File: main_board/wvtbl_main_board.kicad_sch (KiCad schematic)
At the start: 12 parts, among them J101 V/Oct, J102 X, J103 Y, J104 Out, J105 Conn_02x08_Odd_Even

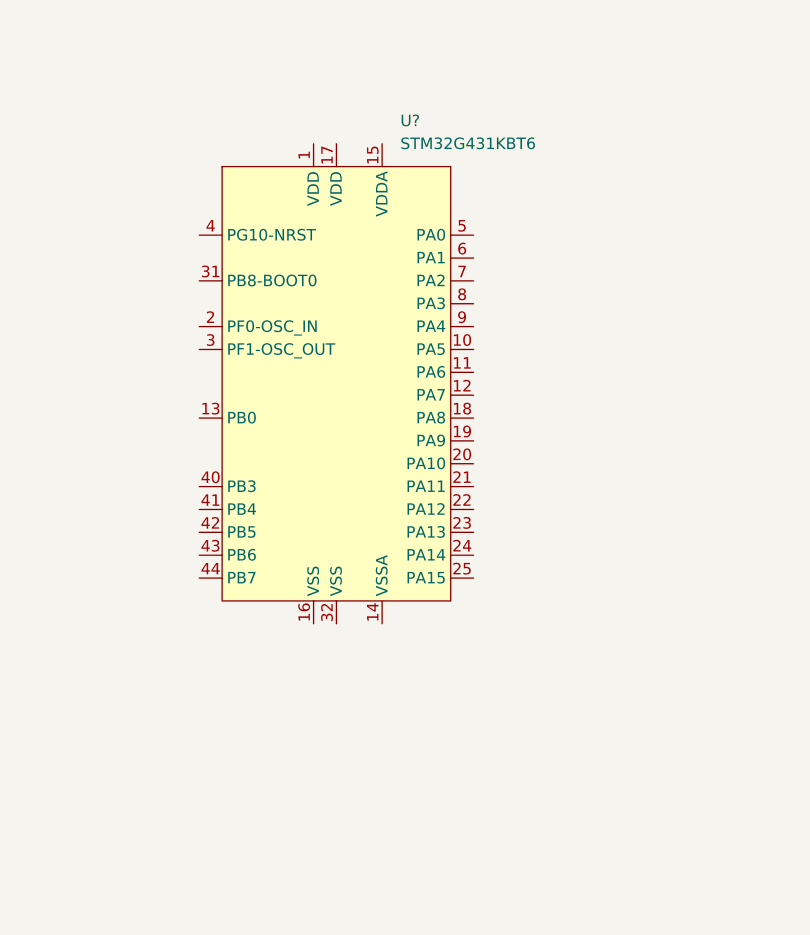
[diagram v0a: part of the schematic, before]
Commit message: 6HP Compute module
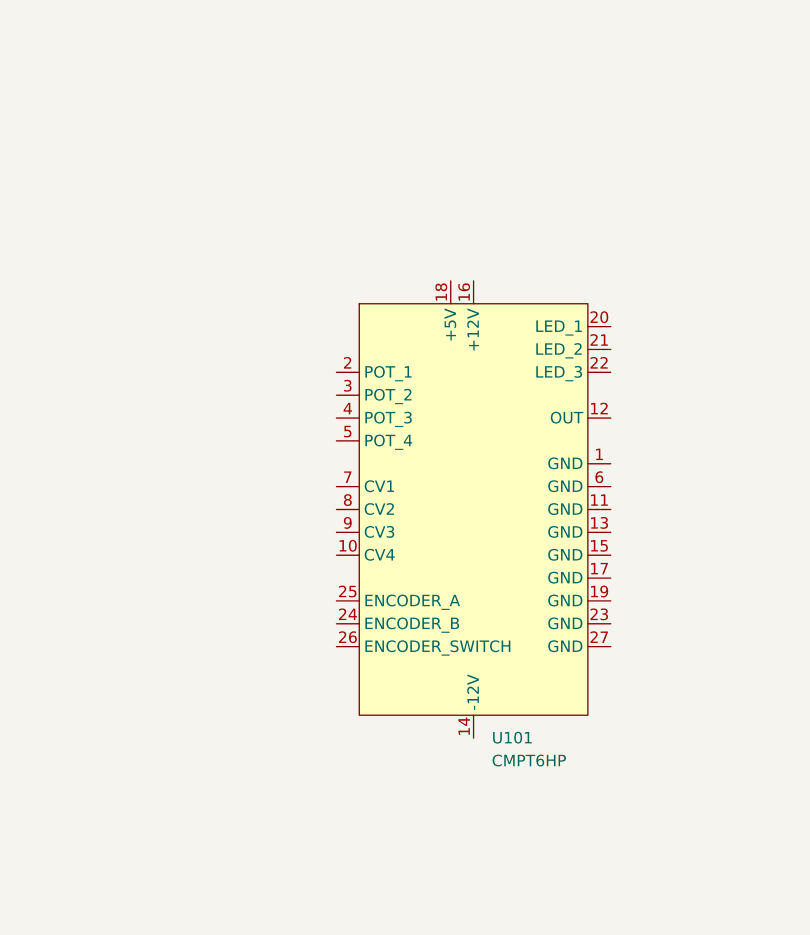
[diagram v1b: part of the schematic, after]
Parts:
- removed U?: STM32G431KBT6, Package_QFP:LQFP-32_7x7mm_P0.8mm, symbol WITNS_ST:STM32G431KBT6
- added U101: CMPT6HP, WITNS:CMPT6HP, symbol WITNS_EURORACK:CMPT6HP
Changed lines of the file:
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@@
     (pin "TN")
   )
-  (symbol (lib_id "Device:R_Potentiometer_Small") (at 106.68 115.57 0) (unit 1)
-    (in_bom yes) (on_board yes) (fields_autoplaced)
-    (property "Reference" "RV102" (id 0) (at 104.14 114.2999 0)
-      (effects (font (size 1.27 1.27)) (justify right))
-    )
-    (property "Value" "100k" (id 1) (at 104.14 116.8399 0)
-      (effects (font (size 1.27 1.27)) (justify right))
-    )
-    (property "Footprint" "WITNS:Potentiometer_Alpha_RD901F-40-00D_Single_Vertical" (id 2) (at 106.68 115.57 0)
-      (effects (font (size 1.27 1.27)) hide)
-    )
-    (property "Datasheet" "~" (id 3) (at 106.68 115.57 0)
-      (effects (font (size 1.27 1.27)) hide)
-    )
-    (pin "1")
-    (pin "2")
-    (pin "3")
-  )
-  (symbol (lib_id "Connector_Generic:Conn_02x08_Odd_Even") (at 50.8 151.13 0) (unit 1)
-    (in_bom yes) (on_board yes) (fields_autoplaced)
-    (property "Reference" "J105" (id 0) (at 52.07 137.16 0))
-    (property "Value" "Conn_02x08_Odd_Even" (id 1) (at 52.07 139.7 0))
-    (property "Footprint" "Connector_PinHeader_2.54mm:PinHeader_2x08_P2.54mm_Vertical_SMD" (id 2) (at 50.8 151.13 0)
-      (effects (font (size 1.27 1.27)) hide)
-    )
-    (property "Datasheet" "~" (id 3) (at 50.8 151.13 0)
-      (effects (font (size 1.27 1.27)) hide)
-    )
-    (pin "1")
-    (pin "10")
-    (pin "11")
-    (pin "12")
-    (pin "13")
-    (pin "14")
-    (pin "15")
-    (pin "16")
-    (pin "2")
-    (pin "3")
-    (pin "4")
-    (pin "5")
-    (pin "6")
-    (pin "7")
-    (pin "8")
-    (pin "9")
-  )
-  (symbol (lib_id "Connector:AudioJack2_SwitchT") (at 120.65 138.43 0) (unit 1)
-    (in_bom yes) (on_board yes) (fields_autoplaced)
-    (property "Reference" "J102" (id 0) (at 120.015 129.54 0))
-    (property "Value" "X" (id 1) (at 120.015 132.08 0))
-    (property "Footprint" "WITNS:Jack_3.5mm_QingPu_WQP-PJ398SM_Vertical_CircularHoles" (id 2) (at 120.65 138.43 0)
-      (effects (font (size 1.27 1.27)) hide)
-    )
-    (property "Datasheet" "~" (id 3) (at 120.65 138.43 0)
-      (effects (font (size 1.27 1.27)) hide)
-    )
-    (pin "S")
-    (pin "T")
-    (pin "TN")
-  )
-  (symbol (lib_id "WITNS_ST:STM32G431KBT6") (at 182.88 57.15 0) (unit 1)
-    (in_bom yes) (on_board yes) (fields_autoplaced)
-    (property "Reference" "U?" (id 0) (at 189.9794 27.94 0)
+  (symbol (lib_id "WITNS_EURORACK:CMPT6HP") (at 198.12 52.07 0) (unit 1)
+    (in_bom yes) (on_board yes) (fields_autoplaced)
+    (property "Reference" "U101" (id 0) (at 200.1394 96.52 0)
       (effects (font (size 1.27 1.27)) (justify left))
     )
-    (property "Value" "STM32G431KBT6" (id 1) (at 189.9794 30.48 0)
+    (property "Value" "CMPT6HP" (id 1) (at 200.1394 99.06 0)
       (effects (font (size 1.27 1.27)) (justify left))
     )
-    (property "Footprint" "Package_QFP:LQFP-32_7x7mm_P0.8mm" (id 2) (at 182.88 96.52 0)
-      (effects (font (size 1.27 1.27)) hide)
-    )
-    (property "Datasheet" "" (id 3) (at 182.88 99.06 0)
+    (property "Footprint" "WITNS:CMPT6HP" (id 2) (at 208.28 96.52 0)
+      (effects (font (size 1.27 1.27)) hide)
+    )
+    (property "Datasheet" "" (id 3) (at 198.12 53.34 0)
       (effects (font (size 1.27 1.27)) hide)
     )
@@
     (pin "24")
     (pin "25")
-    (pin "3")
-    (pin "31")
-    (pin "32")
+    (pin "26")
+    (pin "27")
+    (pin "3")
     (pin "4")
-    (pin "40")
-    (pin "41")
-    (pin "42")
-    (pin "43")
-    (pin "44")
     (pin "5")
     (pin "6")
@@
     (pin "9")
   )
+  (symbol (lib_id "Device:R_Potentiometer_Small") (at 106.68 115.57 0) (unit 1)
+    (in_bom yes) (on_board yes) (fields_autoplaced)
+    (property "Reference" "RV102" (id 0) (at 104.14 114.2999 0)
+      (effects (font (size 1.27 1.27)) (justify right))
+    )
+    (property "Value" "100k" (id 1) (at 104.14 116.8399 0)
+      (effects (font (size 1.27 1.27)) (justify right))
+    )
+    (property "Footprint" "WITNS:Potentiometer_Alpha_RD901F-40-00D_Single_Vertical" (id 2) (at 106.68 115.57 0)
+      (effects (font (size 1.27 1.27)) hide)
+    )
+    (property "Datasheet" "~" (id 3) (at 106.68 115.57 0)
+      (effects (font (size 1.27 1.27)) hide)
+    )
+    (pin "1")
+    (pin "2")
+    (pin "3")
+  )
+  (symbol (lib_id "Connector_Generic:Conn_02x08_Odd_Even") (at 50.8 151.13 0) (unit 1)
+    (in_bom yes) (on_board yes) (fields_autoplaced)
+    (property "Reference" "J105" (id 0) (at 52.07 137.16 0))
+    (property "Value" "Conn_02x08_Odd_Even" (id 1) (at 52.07 139.7 0))
+    (property "Footprint" "Connector_PinHeader_2.54mm:PinHeader_2x08_P2.54mm_Vertical_SMD" (id 2) (at 50.8 151.13 0)
+      (effects (font (size 1.27 1.27)) hide)
+    )
+    (property "Datasheet" "~" (id 3) (at 50.8 151.13 0)
+      (effects (font (size 1.27 1.27)) hide)
+    )
+    (pin "1")
+    (pin "10")
+    (pin "11")
+    (pin "12")
+    (pin "13")
+    (pin "14")
+    (pin "15")
+    (pin "16")
+    (pin "2")
+    (pin "3")
+    (pin "4")
+    (pin "5")
+    (pin "6")
+    (pin "7")
+    (pin "8")
+    (pin "9")
+  )
+  (symbol (lib_id "Connector:AudioJack2_SwitchT") (at 120.65 138.43 0) (unit 1)
+    (in_bom yes) (on_board yes) (fields_autoplaced)
+    (property "Reference" "J102" (id 0) (at 120.015 129.54 0))
+    (property "Value" "X" (id 1) (at 120.015 132.08 0))
+    (property "Footprint" "WITNS:Jack_3.5mm_QingPu_WQP-PJ398SM_Vertical_CircularHoles" (id 2) (at 120.65 138.43 0)
+      (effects (font (size 1.27 1.27)) hide)
+    )
+    (property "Datasheet" "~" (id 3) (at 120.65 138.43 0)
+      (effects (font (size 1.27 1.27)) hide)
+    )
+    (pin "S")
+    (pin "T")
+    (pin "TN")
+  )
   (symbol (lib_id "WITNS_EURORACK:ENCODER-RGB-SWITCH") (at 82.55 78.74 0) (unit 1)
     (in_bom yes) (on_board yes) (fields_autoplaced)
@@
       (reference "S101") (unit 1) (value "ENCODER-RGB-SWITCH") (footprint "WITNS:ENCODER_LED_3")
     )
-    (path "/c052cb67-b420-449e-969a-d1abb56289fe"
-      (reference "U?") (unit 1) (value "STM32G431KBT6") (footprint "Package_QFP:LQFP-32_7x7mm_P0.8mm")
-    )
-  )
+    (path "/52aaa45a-89d2-4d44-ab94-385a955b0812"
+      (reference "U101") (unit 1) (value "CMPT6HP") (footprint "WITNS:CMPT6HP")
+    )
+  )

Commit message: Main board PCB
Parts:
- removed J102: X, WITNS:Jack_3.5mm_QingPu_WQP-PJ398SM_Vertical_CircularHoles, symbol Connector:AudioJack2_SwitchT
- removed J103: Y, WITNS:Jack_3.5mm_QingPu_WQP-PJ398SM_Vertical_CircularHoles, symbol Connector:AudioJack2_SwitchT
- removed RV102, RV103, RV104: 100k, WITNS:Potentiometer_Alpha_RD901F-40-00D_Single_Vertical, symbol Device:R_Potentiometer_Small
- added C1, C4: 10nF, Capacitor_SMD:C_0603_1608Metric, symbol Device:C_Small
- added C10, C12, C8: 10uF, Capacitor_SMD:CP_Elec_4x5.4, symbol Device:C_Polarized_Small
- added C11, C13, C2, C3, C5, C6, C7, C9: 100nF, Capacitor_SMD:C_0603_1608Metric, symbol Device:C_Small
- added D1, D2, D3, D4: TVS 15V, Diode_SMD:D_SMA, symbol Device:D_TVS_Filled
- added J3: X, WITNS:Jack_3.5mm_QingPu_WQP-PJ398SM_Vertical_CircularHoles, symbol Connector:AudioJack2_SwitchT
- added J4: Y, WITNS:Jack_3.5mm_QingPu_WQP-PJ398SM_Vertical_CircularHoles, symbol Connector:AudioJack2_SwitchT
- added R1, R2, R3, R4, R5: 10k, Resistor_SMD:R_0603_1608Metric, symbol Device:R_Small
- added R6, R7, R8: 100R, Resistor_SMD:R_0603_1608Metric, symbol Device:R_Small
- added RV2, RV3, RV4: 100k, WITNS:Potentiometer_Alpha_RD901F-40-00D_Single_Vertical, symbol Device:R_Potentiometer_Small
- J1: renamed from J105; value Conn_02x08_Odd_Even -> POWER
- renumbered J101 to J2, J104 to J5, RV101 to RV1, S101 to S1, U101 to U1
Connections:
- net GND: now reaches J2.S
- net GND: now also J1.10 (Pin_10), J1.11 (Pin_11), J1.12 (Pin_12), J1.13 (Pin_13), J1.14 (Pin_14), J1.9 (Pin_9), J2.TN, J5.S, RV1.3, S1.C, U1.1 (GND), U1.10 (CV4), U1.11 (GND), U1.13 (GND), U1.15 (GND), U1.17 (GND), U1.19 (GND), U1.23 (GND), C1.2, C10.2, C11.2, C12.2, C13.2, C2.2, C3.2, C4.2, C5.2, C6.2, C7.2, C8.1, C9.1, D1.1 (A1), D2.1 (A1), D3.1 (A1), D4.1 (A1), J3.S, J3.TN, J4.S, J4.TN, R5.1, RV2.3, RV3.3, RV4.3
- net CV1: now reaches J2.T
- net CV1: now also U1.7 (CV1), D1.2 (A2)
- net OUT: now reaches U1.12 (OUT)
- net OUT: now also J5.T, D3.2 (A2)
- net -12V: now reaches U1.14 (-12V)
- net -12V: now also J1.15 (Pin_15), J1.16 (Pin_16), C8.2, C9.2
- net +12V: now reaches U1.16 (+12V)
- net +12V: now also J1.7 (Pin_7), J1.8 (Pin_8), C10.1, C11.1
- net +5V: now reaches U1.18 (+5V)
- net +5V: now also J1.5 (Pin_5), J1.6 (Pin_6), C12.1, C13.1
- net POT_1: now reaches U1.2 (POT_1)
- net POT_1: now also RV1.2, C2.1
- net LED_1: now reaches U1.20 (LED_1)
- net LED_1: now also R8.2
- net LED_2: now reaches U1.21 (LED_2)
- net LED_2: now also R7.2
- net LED_3: now reaches U1.22 (LED_3)
- net LED_3: now also R6.2
- net ENCODER_B: now reaches U1.24 (ENCODER_B)
- net ENCODER_B: now also C4.1, R2.1
- net ENCODER_A: now reaches U1.25 (ENCODER_A)
- net ENCODER_A: now also C1.1, R1.1
- net ENCODER_SWITCH: now reaches U1.26 (ENCODER_SWITCH)
- net ENCODER_SWITCH: now also S1.3, R5.2
- net +3.3V: now reaches U1.27 (+3.3V)
- net +3.3V: now also S1.5, C3.1, R3.1, R4.1
- net POT_2: now reaches U1.3 (POT_2)
- net POT_2: now also C5.1, RV2.2
- net POT_3: now reaches U1.4 (POT_3)
- net POT_3: now also C6.1, RV3.2
- net POT_4: now reaches U1.5 (POT_4)
- net POT_4: now also C7.1, RV4.2
- net +3.3VA: now reaches U1.6 (+3.3VA)
- net +3.3VA: now also RV1.1, RV2.1, RV3.1, RV4.1
- net CV2: now reaches U1.8 (CV2)
- net CV2: now also D2.2 (A2), J3.T
- net CV3: now reaches U1.9 (CV3)
- net CV3: now also D4.2 (A2), J4.T
- net at S1.1: now also R6.1
- net at S1.2: now also R7.1
- net at S1.4: now also R8.1
- net at S1.A: now also R1.2, R3.2
- net at S1.B: now also R2.2, R4.2
- no-connect marks 0 -> 5
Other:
- moved on the sheet: J1, J2, J5, RV1, S1
